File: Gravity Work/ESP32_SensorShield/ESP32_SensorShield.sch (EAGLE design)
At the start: 28 parts, among them IC1 BMP388, U1 FGPMMOPA6H, Y1 32.768kHz

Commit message: V1 dev
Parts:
- added J1, J2: (no value), SparkFun-Connectors:CONN_04SMD2
- added J3: (no value), SparkFun-Connectors:JST_2MM_MALE
- added U2: MB85RC256VPF-G-JNERE2, microbuilder:FRAM_SOIC8_I2C
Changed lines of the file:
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@@
 <?xml version="1.0" encoding="utf-8"?>
 <!DOCTYPE eagle SYSTEM "eagle.dtd">
-<eagle version="8.7.1">
+<eagle version="9.0.1">
 <drawing>
 <settings>
@@
 <setting verticaltext="up"/>
 </settings>
-<grid distance="0.05" unitdist="inch" unit="inch" style="lines" multiple="1" display="no" altdistance="0.01" altunitdist="inch" altunit="inch"/>
+<grid distance="0.1" unitdist="inch" unit="inch" style="lines" multiple="1" display="no" altdistance="0.01" altunitdist="inch" altunit="inch"/>
 <layers>
 <layer number="1" name="Top" color="4" fill="1" visible="no" active="no"/>
@@
 <part name="U$14" library="microbuilder" deviceset="3.3V" device=""/>
 <part name="U$15" library="microbuilder" deviceset="GND" device=""/>
+<part name="J1" library="SparkFun-Connectors" library_urn="urn:adsk.eagle:library:513" deviceset="CONN_04" device="SMD2" package3d_urn="urn:adsk.eagle:package:38096/1"/>
+<part name="J2" library="SparkFun-Connectors" library_urn="urn:adsk.eagle:library:513" deviceset="CONN_04" device="SMD2" package3d_urn="urn:adsk.eagle:package:38096/1"/>
+<part name="J3" library="SparkFun-Connectors" library_urn="urn:adsk.eagle:library:513" deviceset="JST_2MM_MALE" device="" package3d_urn="urn:adsk.eagle:package:38042/1"/>
+<part name="U2" library="microbuilder" deviceset="FRAM_SOIC8_I2C" device="" value="MB85RC256VPF-G-JNERE2"/>
 </parts>
 <sheets>
@@
 <instance part="U$14" gate="G$1" x="2.54" y="64.77"/>
 <instance part="U$15" gate="G$1" x="3.81" y="2.54"/>
+<instance part="J1" gate="G$1" x="332.74" y="55.88"/>
+<instance part="J2" gate="G$1" x="332.74" y="38.1"/>
+<instance part="J3" gate="G$1" x="6.35" y="100.33" rot="R90"/>
+<instance part="U2" gate="G$1" x="172.72" y="99.06"/>
 </instances>
 <busses>
@@
 which will not be processed correctly with this version.
 </note>
+<note version="8.2" severity="warning">
+Since Version 8.2, EAGLE supports online libraries. The ids
+of those online libraries will not be understood (or retained)
+with this version.
+</note>
+<note version="8.3" severity="warning">
+Since Version 8.3, EAGLE supports URNs for individual library
+assets (packages, symbols, and devices). The URNs of those assets
+will not be understood (or retained) with this version.
+</note>
+<note version="8.3" severity="warning">
+Since Version 8.3, EAGLE supports the association of 3D packages
+with devices in libraries, schematics, and board files. Those 3D
+packages will not be understood (or retained) with this version.
+</note>
 </compatibility>

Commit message: Added DC2DC Conv, EEPROM, Got rid of Coin Cell, Added Switch
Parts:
- removed B1: CR1220, microbuilder:BATTERYCR1220_SMT
- removed J1, J2: (no value), SparkFun-Connectors:CONN_04SMD2
- removed U$45: U.FL, microbuilder:U.FL
- added C11, C12, C8, C9: 10uF, microbuilder:CAP_CERAMIC0805
- added R4: 10K, microbuilder:RESISTOR0603
- added S1: EG1213, adafruit:EG1213
- added U3: SPX3819-3.3, microbuilder:VREG_SOT23-5
- added X1: (no value), adafruit:SMACONNECTOR_EDGE
- D2: value CUS520 -> MBR120; device microbuilder:DIODESOD-323 -> microbuilder:DIODE-SCHOTTKYSOD-123
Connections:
- removed net N$7: B1.+, D2.A
- new net AUX_3V3: C11.P$1, C12.P$1, U3.OUT
- new net N$11: R4.2, U3.EN
- new net VBAT: D2.A, S11.O, U$1.BAT
- new net VUSB: C9.P$1, D2.C, R4.1, U3.IN
- net 3.3V: now also C8.P$1, U2.VCC
- net GND: now also C11.P$2, C12.P$2, C8.P$2, C9.P$2, J3.-, U2.GND, U3.GND, X1.GND3, X1.GND4; no longer B1.-, U$45.GND@0, U$45.GND@1
- net N$3: now also X1.ANT; no longer U$45.SIGNAL
- net N$6: now also J3.+, S11.P; no longer D2.C, U1.VBACKUP
- net SCL: now also U2.SCL
- net SDA: now also U2.SDA
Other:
- note added: "DC/DC CONV."
- note added: "EEPROM"
- moved on the sheet: J3, U2

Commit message: Add Communication Pins, Need to connect headers to signals.
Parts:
- added C13: 10uF, microbuilder:CAP_CERAMIC0805
- added J1, J2: (no value), SparkFun-Connectors:CONN_04
- added J6: (no value), SparkFun-Connectors:CONN_02
- added J7: 2X6 FEMALE, SparkFun-Connectors:CONN_06X2PTH_FEMALE
- added R7: 10k, microbuilder:RESISTOR0603
- added U4: SN65HVD230D, SN65HVD230D:SN65HVD230D
- C12: value 10uF -> 0.1uF
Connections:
- new net CANH: U4.CANH
- new net CANL: U4.CANL
- new net CAN_RX: U4.R
- new net CAN_TX: U4.D
- new net GPIO36: U$1.A4
- new net GPIO4: U$1.A5
- new net N$10: R7.2, U4.RS
- new net N$7: C13.P$1, U4.VCC
- net GND: now also C13.P$2, R7.1, U4.GND
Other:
- note added: "CAN BUS COMM."
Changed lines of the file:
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@@
 <part name="U$32" library="microbuilder" deviceset="GND" device=""/>
 <part name="C11" library="microbuilder" deviceset="CAP_CERAMIC" device="0805" value="10uF"/>
-<part name="C12" library="microbuilder" deviceset="CAP_CERAMIC" device="0805" value="10uF"/>
+<part name="C12" library="microbuilder" deviceset="CAP_CERAMIC" device="0805" value="0.1uF"/>
 <part name="U$33" library="microbuilder" deviceset="GND" device=""/>
 <part name="U$34" library="microbuilder" deviceset="GND" device=""/>
+<part name="J1" library="SparkFun-Connectors" library_urn="urn:adsk.eagle:library:513" deviceset="CONN_04" device="" package3d_urn="urn:adsk.eagle:package:38085/1"/>
+<part name="J2" library="SparkFun-Connectors" library_urn="urn:adsk.eagle:library:513" deviceset="CONN_04" device="" package3d_urn="urn:adsk.eagle:package:38085/1"/>
+<part name="U4" library="SN65HVD230D" deviceset="SN65HVD230D" device=""/>
+<part name="C13" library="microbuilder" deviceset="CAP_CERAMIC" device="0805" value="10uF"/>
+<part name="U$35" library="microbuilder" deviceset="GND" device=""/>
+<part name="R7" library="microbuilder" deviceset="RESISTOR" device="0603" value="10k"/>
+<part name="J6" library="SparkFun-Connectors" library_urn="urn:adsk.eagle:library:513" deviceset="CONN_02" device="" package3d_urn="urn:adsk.eagle:package:38039/1"/>
+<part name="J7" library="SparkFun-Connectors" library_urn="urn:adsk.eagle:library:513" deviceset="CONN_06X2" device="PTH_FEMALE" package3d_urn="urn:adsk.eagle:package:38277/1" value="2X6 FEMALE"/>
 </parts>
 <sheets>
@@
 <text x="346.71" y="69.85" size="2.54" layer="94">EEPROM </text>
 <wire x1="-7.62" y1="143.51" x2="-7.62" y2="76.2" width="0.1524" layer="94"/>
-<wire x1="-7.62" y1="76.2" x2="55.88" y2="76.2" width="0.1524" layer="94"/>
-<wire x1="55.88" y1="76.2" x2="55.88" y2="143.51" width="0.1524" layer="94"/>
-<wire x1="55.88" y1="143.51" x2="-7.62" y2="143.51" width="0.1524" layer="94"/>
+<wire x1="-7.62" y1="76.2" x2="57.15" y2="76.2" width="0.1524" layer="94"/>
+<wire x1="57.15" y1="76.2" x2="57.15" y2="143.51" width="0.1524" layer="94"/>
+<wire x1="57.15" y1="143.51" x2="-7.62" y2="143.51" width="0.1524" layer="94"/>
 <wire x1="-7.62" y1="143.51" x2="-7.62" y2="151.13" width="0.1524" layer="94"/>
-<wire x1="-7.62" y1="151.13" x2="55.88" y2="151.13" width="0.1524" layer="94"/>
-<wire x1="55.88" y1="151.13" x2="55.88" y2="143.51" width="0.1524" layer="94"/>
-<text x="10.16" y="146.05" size="2.54" layer="94">DC/DC CONV.</text>
+<wire x1="-7.62" y1="151.13" x2="57.15" y2="151.13" width="0.1524" layer="94"/>
+<wire x1="57.15" y1="151.13" x2="57.15" y2="143.51" width="0.1524" layer="94"/>
+<text x="12.7" y="146.05" size="2.54" layer="94">DC/DC CONV.</text>
+<wire x1="58.42" y1="143.51" x2="58.42" y2="76.2" width="0.1524" layer="94"/>
+<wire x1="58.42" y1="76.2" x2="127" y2="76.2" width="0.1524" layer="94"/>
+<wire x1="127" y1="76.2" x2="127" y2="143.51" width="0.1524" layer="94"/>
+<wire x1="127" y1="143.51" x2="58.42" y2="143.51" width="0.1524" layer="94"/>
+<wire x1="58.42" y1="143.51" x2="58.42" y2="151.13" width="0.1524" layer="94"/>
+<wire x1="58.42" y1="151.13" x2="127" y2="151.13" width="0.1524" layer="94"/>
+<wire x1="127" y1="151.13" x2="127" y2="143.51" width="0.1524" layer="94"/>
+<text x="76.2" y="146.05" size="2.54" layer="94">CAN BUS COMM.</text>
 </plain>
 <instances>
@@
 <instance part="U$33" gate="G$1" x="40.64" y="86.36"/>
 <instance part="U$34" gate="G$1" x="49.53" y="86.36"/>
+<instance part="J1" gate="G$1" x="335.28" y="25.4" rot="R180"/>
+<instance part="J2" gate="G$1" x="350.52" y="25.4" rot="R180"/>
+<instance part="U4" gate="A" x="100.33" y="114.3"/>
+<instance part="C13" gate="G$1" x="62.23" y="111.76"/>
+<instance part="U$35" gate="G$1" x="62.23" y="96.52"/>
+<instance part="R7" gate="G$1" x="66.04" y="104.14" smashed="yes" rot="R90">
+<attribute name="NAME" x="64.008" y="102.87" size="1.27" layer="95" font="vector" rot="R90"/>
+<attribute name="VALUE" x="66.675" y="102.87" size="1.27" layer="96" font="vector" rot="R90"/>
+</instance>
+<instance part="J6" gate="G$1" x="337.82" y="7.62" rot="R180"/>
+<instance part="J7" gate="G$1" x="363.22" y="-2.54"/>
 </instances>
 <busses>
@@
 <pinref part="U$34" gate="G$1" pin="GND"/>
 </segment>
+<segment>
+<pinref part="C13" gate="G$1" pin="P$2"/>
+<pinref part="U4" gate="A" pin="GND"/>
+<wire x1="62.23" y1="109.22" x2="62.23" y2="99.06" width="0.1524" layer="91"/>
+<wire x1="62.23" y1="99.06" x2="66.04" y2="99.06" width="0.1524" layer="91"/>
+<pinref part="U$35" gate="G$1" pin="GND"/>
+<junction x="62.23" y="99.06"/>
+<pinref part="R7" gate="G$1" pin="1"/>
+<wire x1="66.04" y1="99.06" x2="82.55" y2="99.06" width="0.1524" layer="91"/>
+<junction x="66.04" y="99.06"/>
+</segment>
 </net>
 <net name="3.3V" class="0">
@@
 </segment>
 </net>
+<net name="GPIO4" class="0">
+<segment>
+<pinref part="U$1" gate="G$1" pin="A5"/>
+<wire x1="40.64" y1="31.75" x2="43.18" y2="31.75" width="0.1524" layer="91"/>
+<label x="43.18" y="31.75" size="1.27" layer="95" xref="yes"/>
+</segment>
+</net>
+<net name="GPIO36" class="0">
+<segment>
+<pinref part="U$1" gate="G$1" pin="A4"/>
+<wire x1="40.64" y1="34.29" x2="43.18" y2="34.29" width="0.1524" layer="91"/>
+<label x="43.18" y="34.29" size="1.27" layer="95" xref="yes"/>
+</segment>
+</net>
+<net name="CAN_TX" class="0">
+<segment>
+<pinref part="U4" gate="A" pin="D"/>
+<wire x1="82.55" y1="114.3" x2="81.28" y2="114.3" width="0.1524" layer="91"/>
+<label x="81.28" y="114.3" size="1.27" layer="95" rot="R180" xref="yes"/>
+</segment>
+</net>
+<net name="CAN_RX" class="0">
+<segment>
+<pinref part="U4" gate="A" pin="R"/>
+<wire x1="82.55" y1="109.22" x2="81.28" y2="109.22" width="0.1524" layer="91"/>
+<label x="81.28" y="109.22" size="1.27" layer="95" rot="R180" xref="yes"/>
+</segment>
+</net>
+<net name="N$7" class="0">
+<segment>
+<pinref part="C13" gate="G$1" pin="P$1"/>
+<pinref part="U4" gate="A" pin="VCC"/>
+<wire x1="62.23" y1="116.84" x2="62.23" y2="124.46" width="0.1524" layer="91"/>
+<wire x1="62.23" y1="124.46" x2="82.55" y2="124.46" width="0.1524" layer="91"/>
+</segment>
+</net>
+<net name="CANL" class="0">
+<segment>
+<pinref part="U4" gate="A" pin="CANL"/>
+<wire x1="118.11" y1="124.46" x2="119.38" y2="124.46" width="0.1524" layer="91"/>
+<label x="119.38" y="124.46" size="1.27" layer="95" xref="yes"/>
+</segment>
+</net>
+<net name="CANH" class="0">
+<segment>
+<pinref part="U4" gate="A" pin="CANH"/>
+<wire x1="118.11" y1="121.92" x2="119.38" y2="121.92" width="0.1524" layer="91"/>
+<label x="119.38" y="121.92" size="1.27" layer="95" xref="yes"/>
+</segment>
+</net>
+<net name="N$10" class="0">
+<segment>
+<pinref part="R7" gate="G$1" pin="2"/>
+<wire x1="66.04" y1="109.22" x2="69.85" y2="109.22" width="0.1524" layer="91"/>
+<wire x1="69.85" y1="109.22" x2="69.85" y2="104.14" width="0.1524" layer="91"/>
+<pinref part="U4" gate="A" pin="RS"/>
+<wire x1="69.85" y1="104.14" x2="82.55" y2="104.14" width="0.1524" layer="91"/>
+</segment>
+</net>

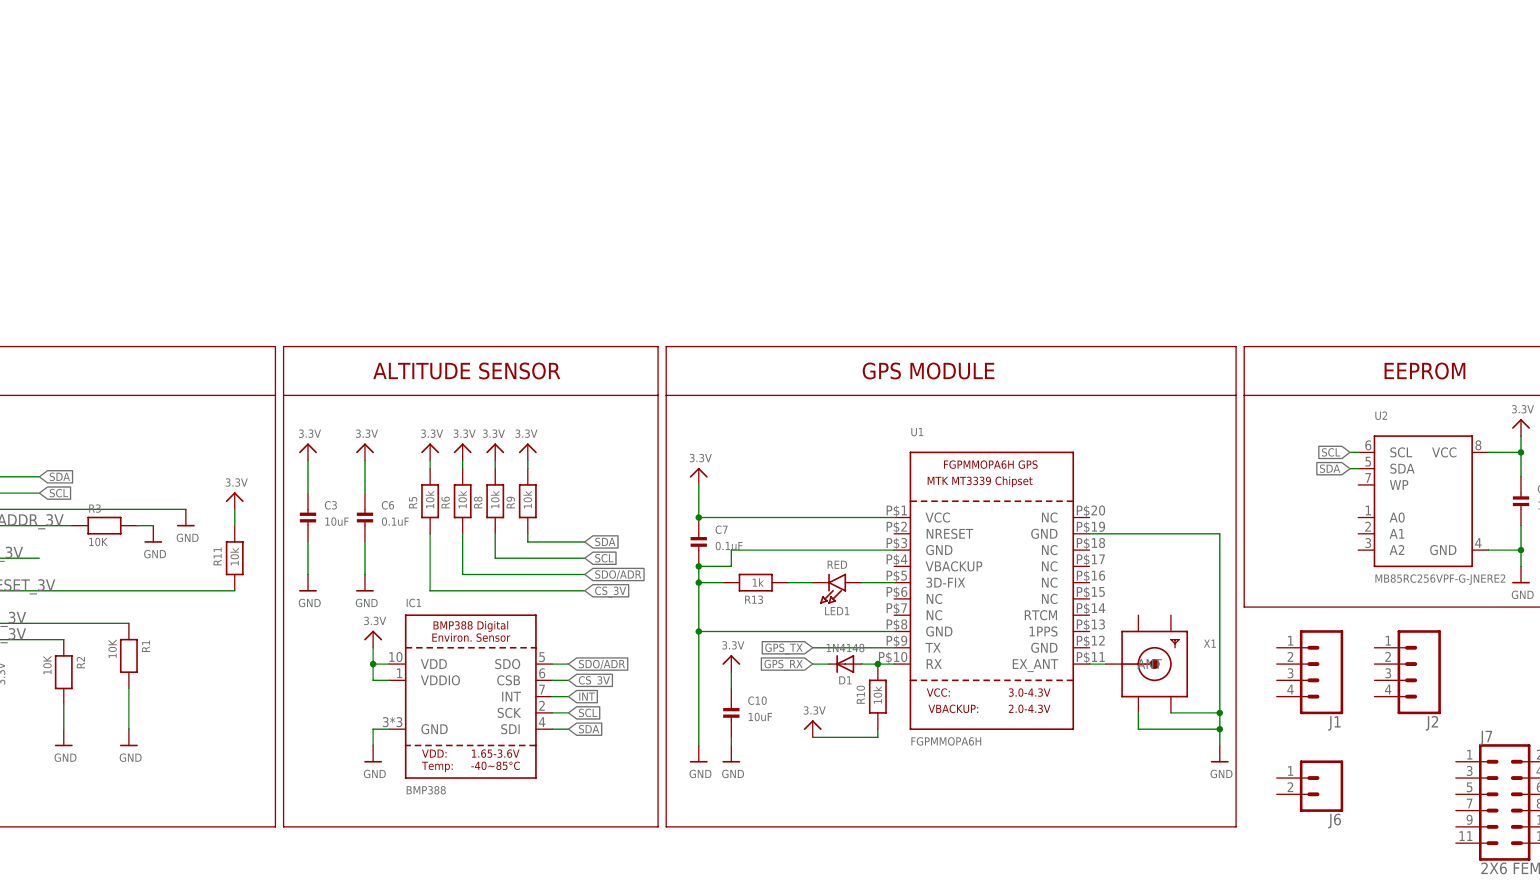
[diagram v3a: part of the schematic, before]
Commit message: Moved Headers, SMA. Added LED.
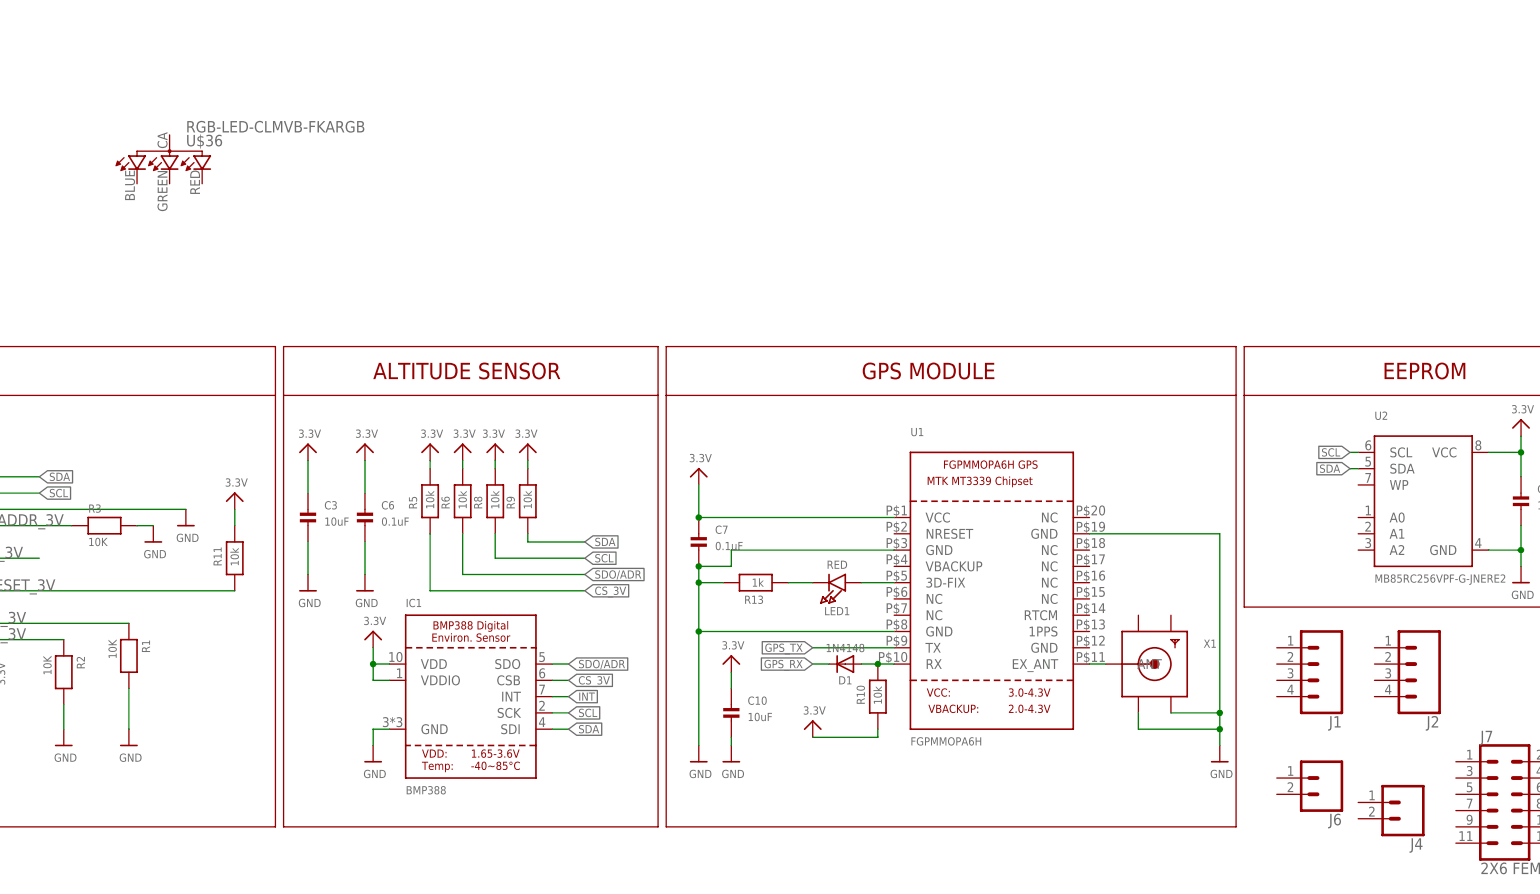
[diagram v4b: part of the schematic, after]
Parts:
- added J4: (no value), SparkFun-Connectors:CONN_02
- added U$36: RGB-LED-CLMVB-FKARGB, Particle:RGB-LED-CLMVB-FKARGB
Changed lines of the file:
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@@
 <?xml version="1.0" encoding="utf-8"?>
 <!DOCTYPE eagle SYSTEM "eagle.dtd">
-<eagle version="8.7.1">
+<eagle version="9.0.1">
 <drawing>
 <settings>
@@
 <layer number="132" name="bAdjust" color="7" fill="1" visible="no" active="yes"/>
 <layer number="133" name="bottom_silk" color="7" fill="1" visible="yes" active="yes"/>
+<layer number="134" name="mbFinish" color="7" fill="1" visible="yes" active="yes"/>
+<layer number="135" name="mtGlue" color="7" fill="1" visible="yes" active="yes"/>
+<layer number="136" name="mbGlue" color="7" fill="1" visible="yes" active="yes"/>
+<layer number="137" name="mtTest" color="7" fill="1" visible="yes" active="yes"/>
+<layer number="138" name="mbTest" color="7" fill="1" visible="yes" active="yes"/>
+<layer number="139" name="mtKeepout" color="7" fill="1" visible="yes" active="yes"/>
+<layer number="140" name="mbKeepout" color="7" fill="1" visible="yes" active="yes"/>
+<layer number="141" name="mtRestrict" color="7" fill="1" visible="yes" active="yes"/>
+<layer number="142" name="mbRestrict" color="7" fill="1" visible="yes" active="yes"/>
+<layer number="143" name="mvRestrict" color="7" fill="1" visible="yes" active="yes"/>
 <layer number="144" name="Drill_legend" color="7" fill="1" visible="no" active="yes"/>
+<layer number="145" name="mHoles" color="7" fill="1" visible="yes" active="yes"/>
+<layer number="146" name="mMilling" color="7" fill="1" visible="yes" active="yes"/>
+<layer number="147" name="mMeasures" color="7" fill="1" visible="yes" active="yes"/>
+<layer number="148" name="mDocument" color="7" fill="1" visible="yes" active="yes"/>
+<layer number="149" name="mReference" color="7" fill="1" visible="yes" active="yes"/>
 <layer number="150" name="Notes" color="7" fill="1" visible="no" active="yes"/>
 <layer number="151" name="HeatSink" color="7" fill="1" visible="no" active="yes"/>
@@
 <layer number="154" name="FabDoc2" color="2" fill="1" visible="no" active="no"/>
 <layer number="155" name="FabDoc3" color="7" fill="15" visible="no" active="no"/>
+<layer number="191" name="mNets" color="7" fill="1" visible="yes" active="yes"/>
+<layer number="192" name="mBusses" color="7" fill="1" visible="yes" active="yes"/>
+<layer number="193" name="mPins" color="7" fill="1" visible="yes" active="yes"/>
+<layer number="194" name="mSymbols" color="7" fill="1" visible="yes" active="yes"/>
+<layer number="195" name="mNames" color="7" fill="1" visible="yes" active="yes"/>
+<layer number="196" name="mValues" color="7" fill="1" visible="yes" active="yes"/>
 <layer number="199" name="Contour" color="7" fill="1" visible="no" active="yes"/>
 <layer number="200" name="200bmp" color="1" fill="10" visible="no" active="yes"/>
@@
 <part name="J6" library="SparkFun-Connectors" library_urn="urn:adsk.eagle:library:513" deviceset="CONN_02" device="" package3d_urn="urn:adsk.eagle:package:38039/1"/>
 <part name="J7" library="SparkFun-Connectors" library_urn="urn:adsk.eagle:library:513" deviceset="CONN_06X2" device="PTH_FEMALE" package3d_urn="urn:adsk.eagle:package:38277/1" value="2X6 FEMALE"/>
+<part name="J4" library="SparkFun-Connectors" library_urn="urn:adsk.eagle:library:513" deviceset="CONN_02" device="" package3d_urn="urn:adsk.eagle:package:38039/1"/>
+<part name="U$36" library="Particle" deviceset="RGB-LED-CLMVB-FKA" device="RGB"/>
 </parts>
 <sheets>
@@
 <instance part="J6" gate="G$1" x="337.82" y="7.62" rot="R180"/>
 <instance part="J7" gate="G$1" x="363.22" y="-2.54"/>
+<instance part="J4" gate="G$1" x="350.52" y="3.81" rot="R180"/>
+<instance part="U$36" gate="G$1" x="157.48" y="105.41"/>
 </instances>
 <busses>
